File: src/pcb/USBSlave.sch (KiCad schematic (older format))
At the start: 0 parts

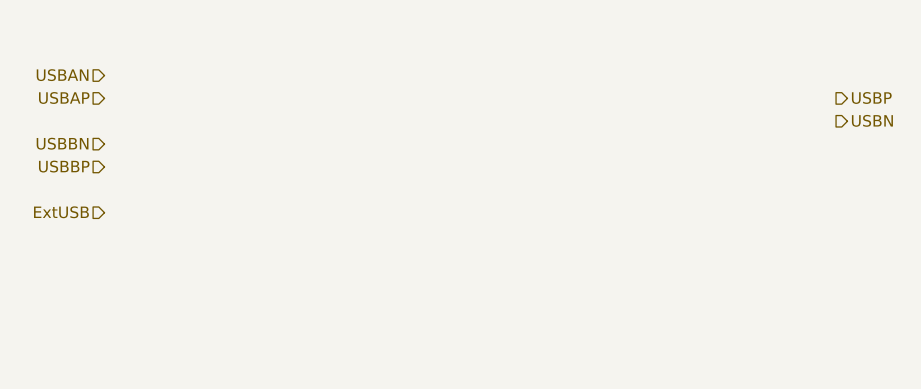
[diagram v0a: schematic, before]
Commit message: added usb demux
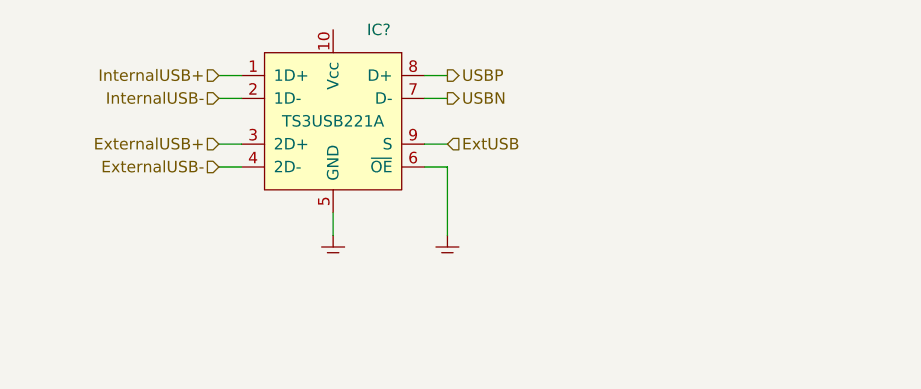
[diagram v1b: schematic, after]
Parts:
- added GND? (x2): GND, symbol Generic:GND
- added IC?: TS3USB221A, symbol USB:TS3USB221A
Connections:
- net ExtUSB: now also IC?.9 (S)
- net USBN: now also IC?.7 (D-)
- net USBP: now also IC?.8 (D+)
- new net: GND?.1 (GND), IC?.5 (GND)
- new net: GND?.1 (GND), IC?.6 (~OE)
- new net ExternalUSB+: IC?.3 (2D+)
- new net ExternalUSB-: IC?.4 (2D-)
- new net InternalUSB+: IC?.1 (1D+)
- new net InternalUSB-: IC?.2 (1D-)
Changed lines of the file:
@@
 Comment4 ""
 $EndDescr
-Text HLabel 4800 4800 0    50   Input ~ 0
+Text HLabel 6300 4500 2    50   Input ~ 0
 ExtUSB
-Text HLabel 8000 4300 2    50   Output ~ 0
+Text HLabel 6300 4200 2    50   Output ~ 0
 USBP
-Text HLabel 8000 4400 2    50   Output ~ 0
+Text HLabel 6300 4300 2    50   Output ~ 0
 USBN
-Text HLabel 4800 4200 0    50   Input ~ 0
-USBAN
-Text HLabel 4800 4300 0    50   Input ~ 0
-USBAP
-Text HLabel 4800 4500 0    50   Input ~ 0
-USBBN
-Text HLabel 4800 4600 0    50   Input ~ 0
-USBBP
+Text HLabel 5300 4300 0    50   Input ~ 0
+InternalUSB-
+Text HLabel 5300 4200 0    50   Input ~ 0
+InternalUSB+
+Text HLabel 5300 4600 0    50   Input ~ 0
+ExternalUSB-
+Text HLabel 5300 4500 0    50   Input ~ 0
+ExternalUSB+
+$Comp
+L USB:TS3USB221A IC?
+U 1 1 5CA87737
+P 5800 4400
+F 0 "IC?" H 5600 4800 50  0000 C CNN
+F 1 "TS3USB221A" H 5800 4400 50  0000 C CNN
+F 2 "" H 5800 4500 50  0001 C CNN
+F 3 "" H 5800 4500 50  0001 C CNN
+	1    5800 4400
+	-1   0    0    -1
+$EndComp
+Wire Wire Line
+	5400 4300 5300 4300
+Wire Wire Line
+	5300 4200 5400 4200
+Wire Wire Line
+	5300 4500 5400 4500
+Wire Wire Line
+	5400 4600 5300 4600
+Wire Wire Line
+	6300 4500 6200 4500
+$Comp
+L Generic:GND GND?
+U 1 1 5CA87909
+P 5800 4900
+F 0 "GND?" H 5950 4950 50  0001 C CNN
+F 1 "GND" H 5950 4900 50  0001 C CNN
+F 2 "" H 5800 4900 50  0001 C CNN
+F 3 "" H 5800 4900 50  0001 C CNN
+	1    5800 4900
+	1    0    0    -1
+$EndComp
+$Comp
+L Generic:GND GND?
+U 1 1 5CA8791D
+P 6300 4900
+F 0 "GND?" H 6450 4950 50  0001 C CNN
+F 1 "GND" H 6450 4900 50  0001 C CNN
+F 2 "" H 6300 4900 50  0001 C CNN
+F 3 "" H 6300 4900 50  0001 C CNN
+	1    6300 4900
+	1    0    0    -1
+$EndComp
+Wire Wire Line
+	6300 4900 6300 4600
+Wire Wire Line
+	6300 4600 6200 4600
+Wire Wire Line
+	5800 4900 5800 4800
+Wire Wire Line
+	6300 4200 6200 4200
+Wire Wire Line
+	6200 4300 6300 4300
 $EndSCHEMATC

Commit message: tweaked libraries
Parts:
- GND? (x2): symbol Generic:GND -> generic:GND
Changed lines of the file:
@@
 	6300 4500 6200 4500
 $Comp
-L Generic:GND GND?
+L generic:GND GND?
 U 1 1 5CA87909
 P 5800 4900
@@
 $EndComp
 $Comp
-L Generic:GND GND?
+L generic:GND GND?
 U 1 1 5CA8791D
 P 6300 4900
